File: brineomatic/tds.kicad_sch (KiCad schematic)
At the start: 4 parts

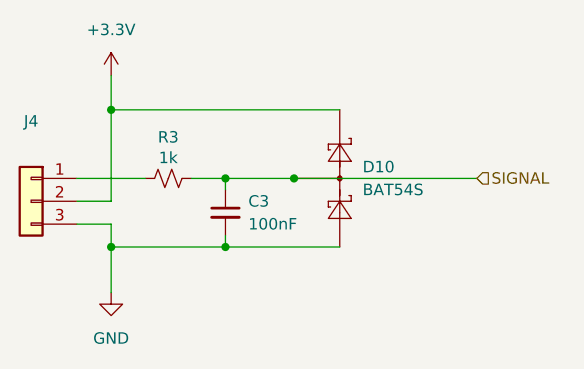
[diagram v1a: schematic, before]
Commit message: tmc2209 driver schematic checked and laid out nicely.
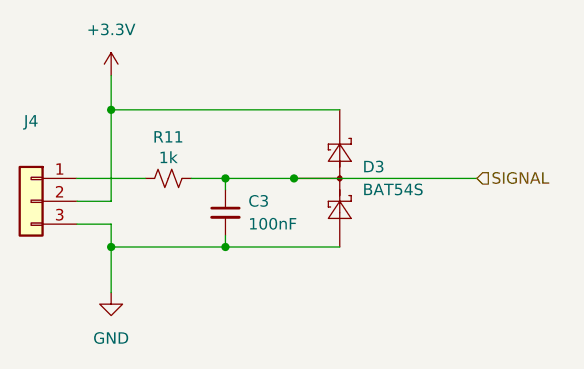
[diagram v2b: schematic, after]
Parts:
- renumbered D10 to D3, R3 to R11
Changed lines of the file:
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@@
 			(project "brineomatic"
 				(path "/96477ae2-ef08-48f3-8dd4-fe4478541f68/4dde40bf-0b86-4621-acd9-eb6c6b71c357"
-					(reference "J14")
+					(reference "J19")
 					(unit 1)
 				)
@@
 		(dnp no)
 		(fields_autoplaced yes)
-		(property "Reference" "#PWR013"
+		(property "Reference" "#PWR015"
 			(at 101.6 77.47 0)
 			(effects
@@
 			(project "brineomatic"
 				(path "/96477ae2-ef08-48f3-8dd4-fe4478541f68/4dde40bf-0b86-4621-acd9-eb6c6b71c357"
-					(reference "#PWR041")
-					(unit 1)
-				)
-				(path "/96477ae2-ef08-48f3-8dd4-fe4478541f68/be3403ab-9eef-436c-86e7-0de3f072ae30"
-					(reference "#PWR013")
+					(reference "#PWR042")
+					(unit 1)
+				)
+				(path "/96477ae2-ef08-48f3-8dd4-fe4478541f68/be3403ab-9eef-436c-86e7-0de3f072ae30"
+					(reference "#PWR015")
 					(unit 1)
 				)
@@
 		(on_board yes)
 		(dnp no)
-		(property "Reference" "R3"
+		(property "Reference" "R11"
 			(at 107.95 80.518 90)
 			(effects
@@
 			(project "brineomatic"
 				(path "/96477ae2-ef08-48f3-8dd4-fe4478541f68/4dde40bf-0b86-4621-acd9-eb6c6b71c357"
-					(reference "R35")
-					(unit 1)
-				)
-				(path "/96477ae2-ef08-48f3-8dd4-fe4478541f68/be3403ab-9eef-436c-86e7-0de3f072ae30"
-					(reference "R3")
+					(reference "R46")
+					(unit 1)
+				)
+				(path "/96477ae2-ef08-48f3-8dd4-fe4478541f68/be3403ab-9eef-436c-86e7-0de3f072ae30"
+					(reference "R11")
 					(unit 1)
 				)
@@
 		(dnp no)
 		(fields_autoplaced yes)
-		(property "Reference" "#PWR014"
+		(property "Reference" "#PWR016"
 			(at 101.6 104.14 0)
 			(effects
@@
 			(project "brineomatic"
 				(path "/96477ae2-ef08-48f3-8dd4-fe4478541f68/4dde40bf-0b86-4621-acd9-eb6c6b71c357"
-					(reference "#PWR042")
-					(unit 1)
-				)
-				(path "/96477ae2-ef08-48f3-8dd4-fe4478541f68/be3403ab-9eef-436c-86e7-0de3f072ae30"
-					(reference "#PWR014")
+					(reference "#PWR043")
+					(unit 1)
+				)
+				(path "/96477ae2-ef08-48f3-8dd4-fe4478541f68/be3403ab-9eef-436c-86e7-0de3f072ae30"
+					(reference "#PWR016")
 					(unit 1)
 				)
@@
 			(project "brineomatic"
 				(path "/96477ae2-ef08-48f3-8dd4-fe4478541f68/4dde40bf-0b86-4621-acd9-eb6c6b71c357"
-					(reference "C21")
+					(reference "C34")
 					(unit 1)
 				)
@@
 		(dnp no)
 		(fields_autoplaced yes)
-		(property "Reference" "D10"
+		(property "Reference" "D3"
 			(at 129.54 83.82 90)
 			(effects
@@
 			(project "brineomatic"
 				(path "/96477ae2-ef08-48f3-8dd4-fe4478541f68/4dde40bf-0b86-4621-acd9-eb6c6b71c357"
-					(reference "D20")
-					(unit 1)
-				)
-				(path "/96477ae2-ef08-48f3-8dd4-fe4478541f68/be3403ab-9eef-436c-86e7-0de3f072ae30"
-					(reference "D10")
-					(unit 1)
-				)
+					(reference "D23")
+					(unit 1)
+				)
+				(path "/96477ae2-ef08-48f3-8dd4-fe4478541f68/be3403ab-9eef-436c-86e7-0de3f072ae30"
+					(reference "D3")
+					(unit 1)
+				)

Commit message: worked on bom for rev b prototype run
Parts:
- C3: LCSC C49678 -> (none)
- J4: LCSC (none) -> C225489
- R11: LCSC C95781 -> (none)
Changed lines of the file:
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@@
 			)
 		)
-		(property "LCSC" ""
+		(property "LCSC" "C225489"
 			(at 92.71 87.63 0)
 			(effects
@@
 			)
 		)
-		(property "LCSC" "C95781"
+		(property "LCSC" ""
 			(at 107.95 85.09 0)
 			(effects
@@
 			)
 		)
-		(property "LCSC" "C49678"
-			(at 114.3 88.9 0)
-			(effects
+		(property "LCSC" ""
+			(at 114.3 88.9 0)
+			(effects

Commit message: updated jlc parts rotations and placement offsets
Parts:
- J4: Rotation Offset (none) -> 270
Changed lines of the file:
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@@
+			)
+		)
+		(property "Rotation Offset" "270"
+			(at 92.71 87.63 0)
+			(effects
+				(font
+					(size 1.27 1.27)
+				)
+				(hide yes)
 			)
 		)

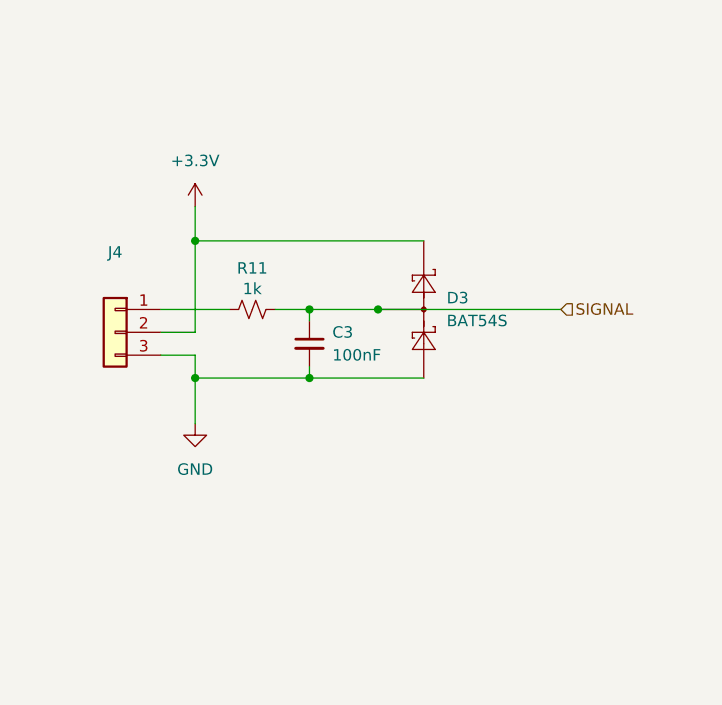
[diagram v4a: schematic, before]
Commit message: added qwiic i2c connector
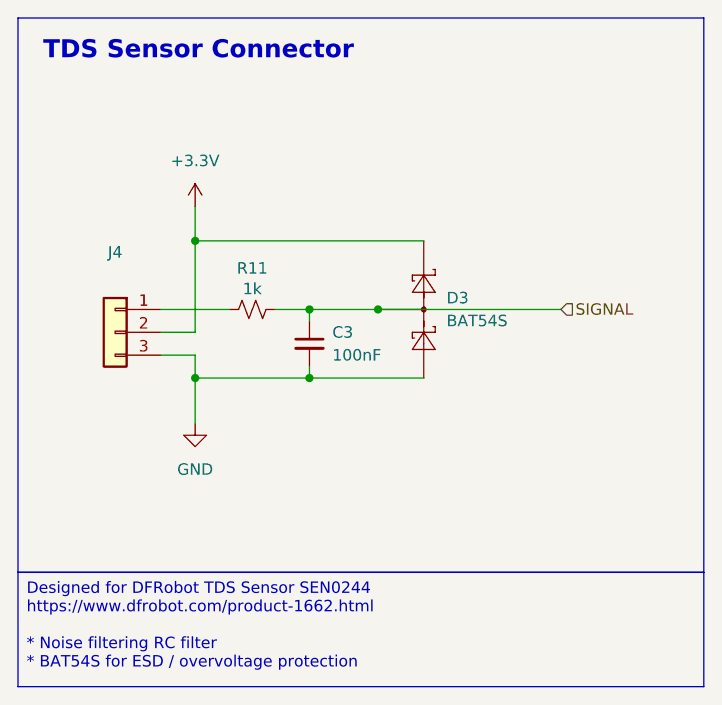
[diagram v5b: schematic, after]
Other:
- note added: "TDS Sensor Connector"
- title: (none) -> https://github.com/hoeken/brineomatic
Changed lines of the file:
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@@
 	(generator_version "9.0")
 	(paper "A4")
+	(title_block
+		(title "https://github.com/hoeken/brineomatic")
+		(date "2025-08-28")
+		(rev "B")
+	)
+	(rectangle
+		(start 81.915 52.705)
+		(end 158.115 114.3)
+		(stroke
+			(width 0)
+			(type default)
+		)
+		(fill
+			(type none)
+		)
+	)
+	(text "TDS Sensor Connector"
+		(exclude_from_sim no)
+		(at 84.709 56.388 0)
+		(effects
+			(font
+				(size 2 2)
+				(thickness 0.4)
+				(bold yes)
+			)
+			(justify left)
+		)
+	)
+	(text_box "Designed for DFRobot TDS Sensor SEN0244\nhttps://www.dfrobot.com/product-1662.html\n\n* Noise filtering RC filter\n* BAT54S for ESD / overvoltage protection"
+		(exclude_from_sim no)
+		(at 81.915 114.3 0)
+		(size 76.2 12.7)
+		(margins 0.9525 0.9525 0.9525 0.9525)
+		(stroke
+			(width 0)
+			(type solid)
+		)
+		(fill
+			(type none)
+		)
+		(effects
+			(font
+				(size 1.27 1.27)
+			)
+			(justify left top)
+		)
+	)
 	(junction
 		(at 114.3 92.71)

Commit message: added pullup resistor to adc alert
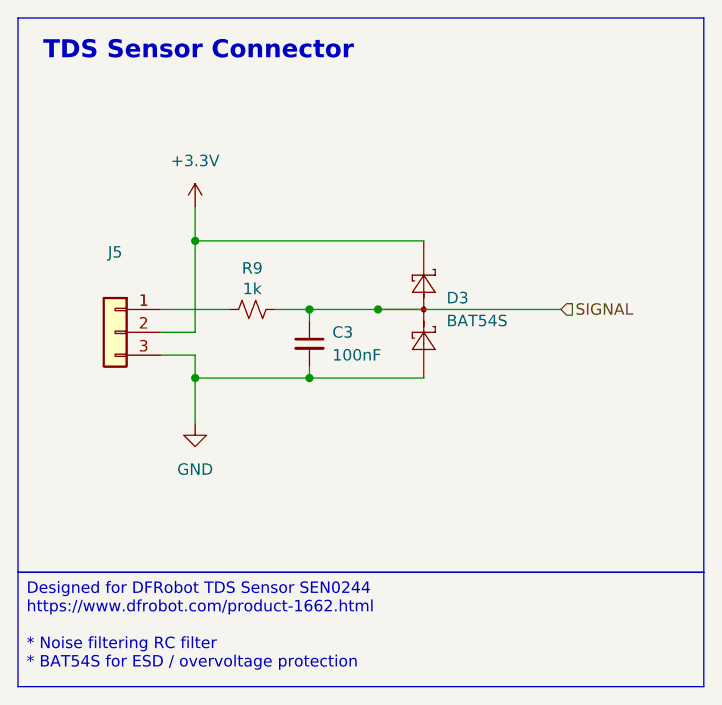
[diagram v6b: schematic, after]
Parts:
- renumbered J4 to J5, R11 to R9
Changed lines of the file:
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@@
 		(dnp no)
 		(fields_autoplaced yes)
-		(property "Reference" "J4"
+		(property "Reference" "J5"
 			(at 92.71 78.74 0)
 			(effects
@@
 			(project "brineomatic"
 				(path "/96477ae2-ef08-48f3-8dd4-fe4478541f68/4dde40bf-0b86-4621-acd9-eb6c6b71c357"
-					(reference "J19")
+					(reference "J20")
 					(unit 1)
 				)
 				(path "/96477ae2-ef08-48f3-8dd4-fe4478541f68/be3403ab-9eef-436c-86e7-0de3f072ae30"
-					(reference "J4")
+					(reference "J5")
 					(unit 1)
 				)
@@
 		(dnp no)
 		(fields_autoplaced yes)
-		(property "Reference" "#PWR015"
+		(property "Reference" "#PWR017"
 			(at 101.6 77.47 0)
 			(effects
@@
 			(project "brineomatic"
 				(path "/96477ae2-ef08-48f3-8dd4-fe4478541f68/4dde40bf-0b86-4621-acd9-eb6c6b71c357"
-					(reference "#PWR042")
+					(reference "#PWR044")
 					(unit 1)
 				)
 				(path "/96477ae2-ef08-48f3-8dd4-fe4478541f68/be3403ab-9eef-436c-86e7-0de3f072ae30"
-					(reference "#PWR015")
+					(reference "#PWR017")
 					(unit 1)
 				)
@@
 		(on_board yes)
 		(dnp no)
-		(property "Reference" "R11"
+		(property "Reference" "R9"
 			(at 107.95 80.518 90)
 			(effects
@@
 				)
 				(path "/96477ae2-ef08-48f3-8dd4-fe4478541f68/be3403ab-9eef-436c-86e7-0de3f072ae30"
-					(reference "R11")
+					(reference "R9")
 					(unit 1)
 				)
@@
 		(dnp no)
 		(fields_autoplaced yes)
-		(property "Reference" "#PWR016"
+		(property "Reference" "#PWR018"
 			(at 101.6 104.14 0)
 			(effects
@@
 			(project "brineomatic"
 				(path "/96477ae2-ef08-48f3-8dd4-fe4478541f68/4dde40bf-0b86-4621-acd9-eb6c6b71c357"
-					(reference "#PWR043")
+					(reference "#PWR045")
 					(unit 1)
 				)
 				(path "/96477ae2-ef08-48f3-8dd4-fe4478541f68/be3403ab-9eef-436c-86e7-0de3f072ae30"
-					(reference "#PWR016")
+					(reference "#PWR018")
 					(unit 1)
 				)
@@
 			(project "brineomatic"
 				(path "/96477ae2-ef08-48f3-8dd4-fe4478541f68/4dde40bf-0b86-4621-acd9-eb6c6b71c357"
-					(reference "C34")
-					(unit 1)
-				)
+					(reference "C35")
+					(unit 1)
+				)

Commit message: stacked tds, removed stepper vref, pulled in esp32-s3 schematic, added extra relay output
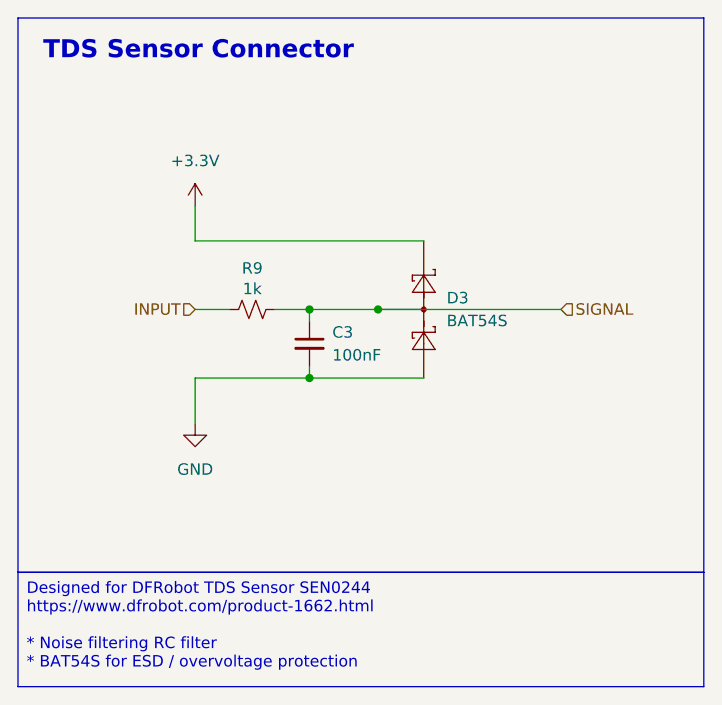
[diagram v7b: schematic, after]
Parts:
- removed J5: ~, Connector_PinHeader_2.54mm:PinHeader_1x03_P2.54mm_Horizontal, symbol Connector_Generic:Conn_01x03
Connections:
- net INPUT: now reaches R9.1
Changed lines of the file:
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@@
 		(color 0 0 0 0)
 	)
-	(junction
-		(at 101.6 77.47)
-		(diameter 0)
-		(color 0 0 0 0)
-	)
-	(junction
-		(at 101.6 92.71)
-		(diameter 0)
-		(color 0 0 0 0)
-	)
-	(wire
-		(pts
-			(xy 101.6 77.47) (xy 101.6 87.63)
-		)
-		(stroke
-			(width 0)
-			(type default)
-		)
-	)
-	(wire
-		(pts
-			(xy 101.6 87.63) (xy 97.79 87.63)
-		)
-		(stroke
-			(width 0)
-			(type default)
-		)
-	)
-	(wire
-		(pts
-			(xy 101.6 90.17) (xy 101.6 92.71)
-		)
-		(stroke
-			(width 0)
-			(type default)
-		)
-	)
-	(wire
-		(pts
-			(xy 97.79 85.09) (xy 105.41 85.09)
+	(wire
+		(pts
+			(xy 101.6 85.09) (xy 105.41 85.09)
 		)
 		(stroke
@@
 	(wire
 		(pts
-			(xy 97.79 90.17) (xy 101.6 90.17)
-		)
-		(stroke
-			(width 0)
-			(type default)
-		)
-	)
-	(wire
-		(pts
 			(xy 114.3 85.09) (xy 114.3 86.36)
 		)
@@
 			(width 0)
 			(type default)
+		)
+	)
+	(hierarchical_label "INPUT"
+		(shape input)
+		(at 101.6 85.09 180)
+		(effects
+			(font
+				(size 1.27 1.27)
+			)
+			(justify right)
 		)
 	)
@@
 			)
 			(justify left)
-		)
-	)
-	(symbol
-		(lib_id "Connector_Generic:Conn_01x03")
-		(at 92.71 87.63 0)
-		(mirror y)
-		(unit 1)
-		(exclude_from_sim no)
-		(in_bom yes)
-		(on_board yes)
-		(dnp no)
-		(fields_autoplaced yes)
-		(property "Reference" "J5"
-			(at 92.71 78.74 0)
-			(effects
-				(font
-					(size 1.27 1.27)
-				)
-			)
-		)
-		(property "Value" "~"
-			(at 92.71 81.28 0)
-			(effects
-				(font
-					(size 1.27 1.27)
-				)
-			)
-		)
-		(property "Footprint" "Connector_PinHeader_2.54mm:PinHeader_1x03_P2.54mm_Horizontal"
-			(at 92.71 87.63 0)
-			(effects
-				(font
-					(size 1.27 1.27)
-				)
-				(hide yes)
-			)
-		)
-		(property "Datasheet" "~"
-			(at 92.71 87.63 0)
-			(effects
-				(font
-					(size 1.27 1.27)
-				)
-				(hide yes)
-			)
-		)
-		(property "Description" "Generic connector, single row, 01x03, script generated (kicad-library-utils/schlib/autogen/connector/)"
-			(at 92.71 87.63 0)
-			(effects
-				(font
-					(size 1.27 1.27)
-				)
-				(hide yes)
-			)
-		)
-		(property "LCSC" "C225489"
-			(at 92.71 87.63 0)
-			(effects
-				(font
-					(size 1.27 1.27)
-				)
-				(hide yes)
-			)
-		)
-		(property "Rotation Offset" "270"
-			(at 92.71 87.63 0)
-			(effects
-				(font
-					(size 1.27 1.27)
-				)
-				(hide yes)
-			)
-		)
-		(pin "3"
-		)
-		(pin "2"
-		)
-		(pin "1"
-		)
-		(instances
-			(project "brineomatic"
-				(path "/96477ae2-ef08-48f3-8dd4-fe4478541f68/4dde40bf-0b86-4621-acd9-eb6c6b71c357"
-					(reference "J20")
-					(unit 1)
-				)
-				(path "/96477ae2-ef08-48f3-8dd4-fe4478541f68/be3403ab-9eef-436c-86e7-0de3f072ae30"
-					(reference "J5")
-					(unit 1)
-				)
-			)
 		)
 	)
@@
 		(dnp no)
 		(fields_autoplaced yes)
-		(property "Reference" "#PWR017"
+		(property "Reference" "#PWR018"
 			(at 101.6 77.47 0)
 			(effects
@@
 			(project "brineomatic"
 				(path "/96477ae2-ef08-48f3-8dd4-fe4478541f68/4dde40bf-0b86-4621-acd9-eb6c6b71c357"
-					(reference "#PWR044")
+					(reference "#PWR058")
 					(unit 1)
 				)
 				(path "/96477ae2-ef08-48f3-8dd4-fe4478541f68/be3403ab-9eef-436c-86e7-0de3f072ae30"
-					(reference "#PWR017")
+					(reference "#PWR018")
 					(unit 1)
 				)
@@
 			(project "brineomatic"
 				(path "/96477ae2-ef08-48f3-8dd4-fe4478541f68/4dde40bf-0b86-4621-acd9-eb6c6b71c357"
-					(reference "R46")
+					(reference "R39")
 					(unit 1)
 				)
@@
 		(dnp no)
 		(fields_autoplaced yes)
-		(property "Reference" "#PWR018"
+		(property "Reference" "#PWR019"
 			(at 101.6 104.14 0)
 			(effects
@@
 			(project "brineomatic"
 				(path "/96477ae2-ef08-48f3-8dd4-fe4478541f68/4dde40bf-0b86-4621-acd9-eb6c6b71c357"
-					(reference "#PWR045")
+					(reference "#PWR059")
 					(unit 1)
 				)
 				(path "/96477ae2-ef08-48f3-8dd4-fe4478541f68/be3403ab-9eef-436c-86e7-0de3f072ae30"
-					(reference "#PWR018")
+					(reference "#PWR019")
 					(unit 1)
 				)
@@
 			(project "brineomatic"
 				(path "/96477ae2-ef08-48f3-8dd4-fe4478541f68/4dde40bf-0b86-4621-acd9-eb6c6b71c357"
-					(reference "C35")
+					(reference "C26")
 					(unit 1)
 				)
@@
 			(project "brineomatic"
 				(path "/96477ae2-ef08-48f3-8dd4-fe4478541f68/4dde40bf-0b86-4621-acd9-eb6c6b71c357"
-					(reference "D23")
-					(unit 1)
-				)
+					(reference "D22")
+					(unit 1)
+				)
